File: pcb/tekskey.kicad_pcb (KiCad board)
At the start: 2 copper layers, 123.8 x 128.6 mm, 97 parts, among them SW0 MX_SW_HS, SW1 MX_SW_HS, SW10 MX_SW_HS, SW11 MX_SW_HS, SW12 MX_SW_HS, SW13 MX_SW_HS, SW14 MX_SW_HS, SW15 MX_SW_HS, SW1B1 MX_SW_HS, SW2 MX_SW_HS, SW20 MX_SW_HS, SW21 MX_SW_HS, SW22 MX_SW_HS, SW23 MX_SW_HS, SW24 MX_SW_HS, SW25 MX_SW_HS, SW2B1 MX_SW_HS, SW3 MX_SW_HS, SW30 MX_SW_HS, SW31 MX_SW_HS, SW32 MX_SW_HS, SW33 MX_SW_HS, SW34 MX_SW_HS, SW35 MX_SW_HS, SW3B1 MX_SW_HS, SW4 MX_SW_HS, SW40 MX_SW_HS, SW41 MX_SW_HS, SW42 MX_SW_HS, SW43 MX_SW_HS, SW44 MX_SW_HS, SW45 MX_SW_HS, SW4B1 MX_SW_HS, SW5 MX_SW_HS, SW50 MX_SW_HS, SW51 MX_SW_HS, SW51B1 MX_SW_HS, SW52 MX_SW_HS, SW53 MX_SW_HS, SW54 MX_SW_HS, SW55 MX_SW_HS, SW55B1 MX_SW_HS, SW5B1 MX_SW_HS

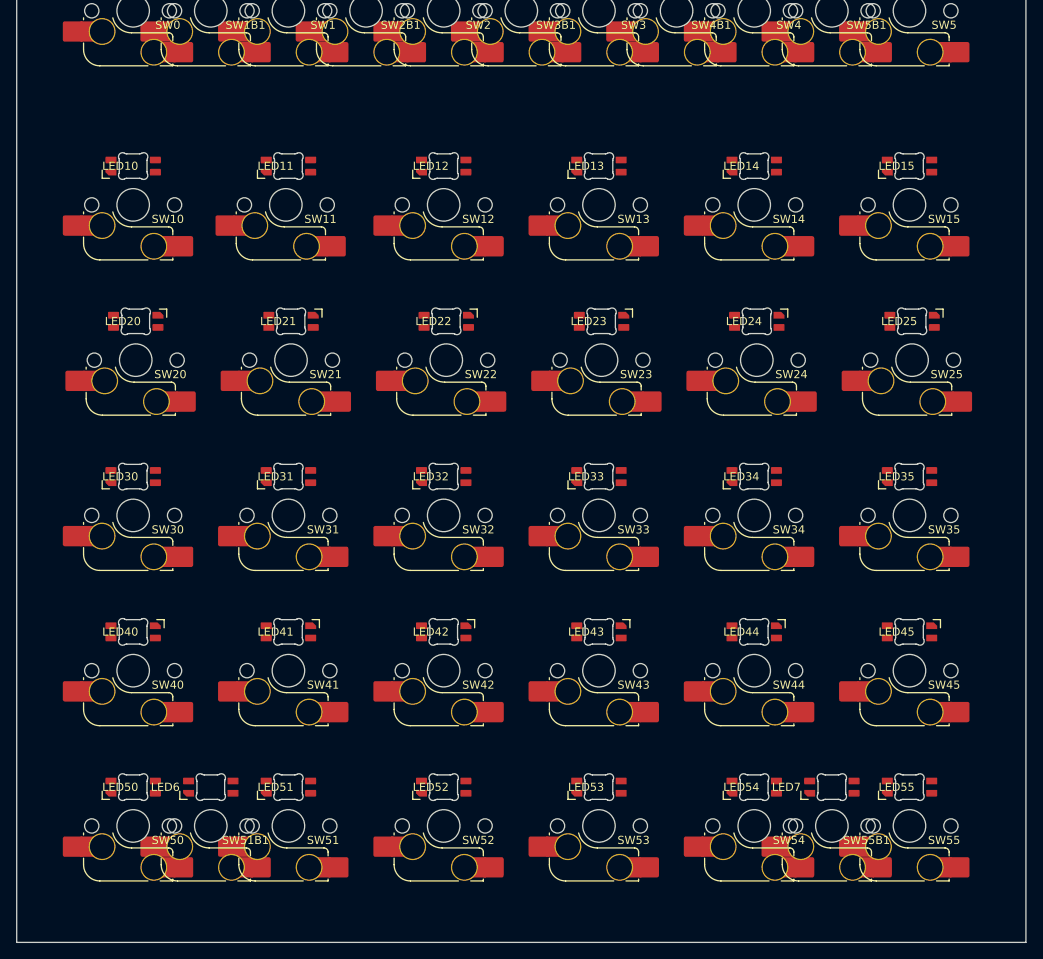
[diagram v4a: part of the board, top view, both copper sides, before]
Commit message: add through hole diodes
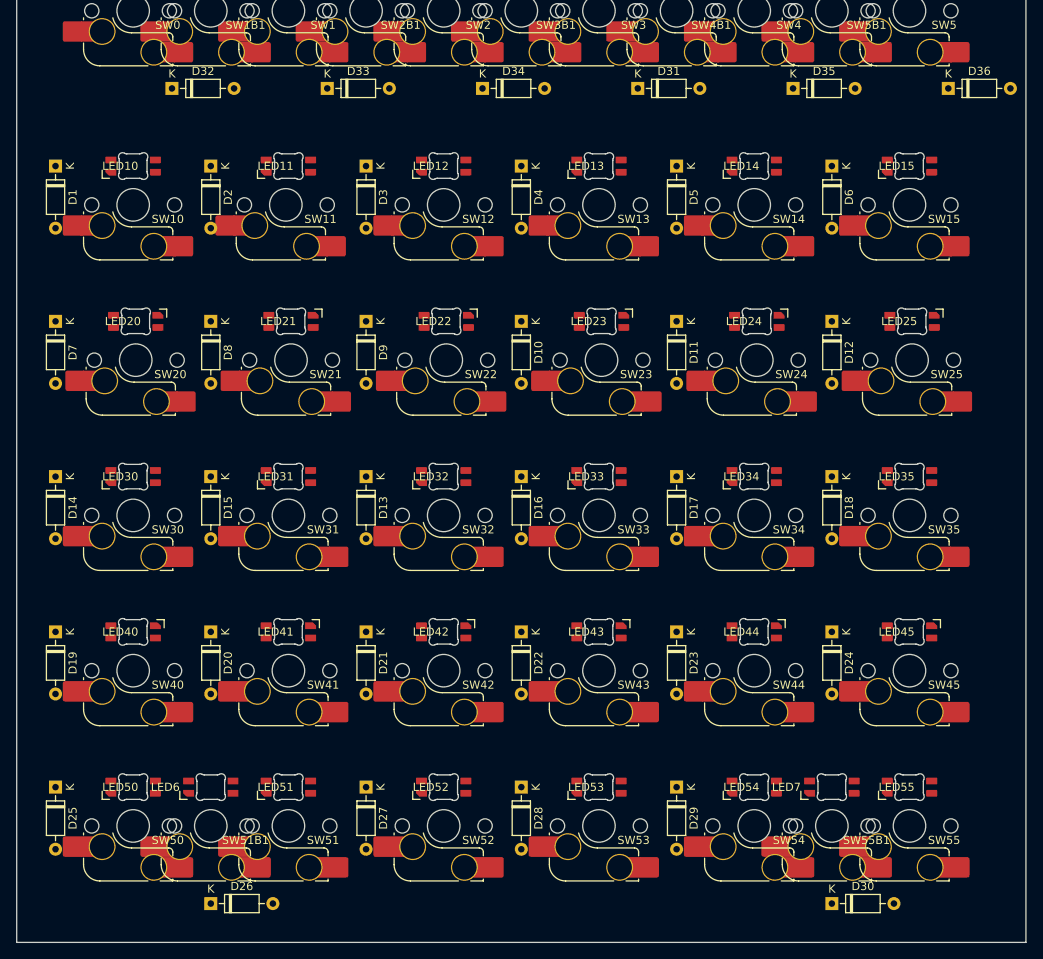
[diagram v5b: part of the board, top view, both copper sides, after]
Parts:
- added D1: 1N4148, Diode_THT:D_DO-35_SOD27_P7.62mm_Horizontal, F.Cu at (38.1, 57.1)
- added D10: 1N4148, Diode_THT:D_DO-35_SOD27_P7.62mm_Horizontal, F.Cu at (95.2, 76.2)
- added D11: 1N4148, Diode_THT:D_DO-35_SOD27_P7.62mm_Horizontal, F.Cu at (114.3, 76.2)
- added D12: 1N4148, Diode_THT:D_DO-35_SOD27_P7.62mm_Horizontal, F.Cu at (133.3, 76.2)
- added D13: 1N4148, Diode_THT:D_DO-35_SOD27_P7.62mm_Horizontal, F.Cu at (76.2, 95.2)
- added D14: 1N4148, Diode_THT:D_DO-35_SOD27_P7.62mm_Horizontal, F.Cu at (38.1, 95.2)
- added D15: 1N4148, Diode_THT:D_DO-35_SOD27_P7.62mm_Horizontal, F.Cu at (57.1, 95.2)
- added D16: 1N4148, Diode_THT:D_DO-35_SOD27_P7.62mm_Horizontal, F.Cu at (95.2, 95.2)
- added D17: 1N4148, Diode_THT:D_DO-35_SOD27_P7.62mm_Horizontal, F.Cu at (114.3, 95.2)
- added D18: 1N4148, Diode_THT:D_DO-35_SOD27_P7.62mm_Horizontal, F.Cu at (133.3, 95.2)
- added D19: 1N4148, Diode_THT:D_DO-35_SOD27_P7.62mm_Horizontal, F.Cu at (38.1, 114.3)
- added D2: 1N4148, Diode_THT:D_DO-35_SOD27_P7.62mm_Horizontal, F.Cu at (57.1, 57.1)
- added D20: 1N4148, Diode_THT:D_DO-35_SOD27_P7.62mm_Horizontal, F.Cu at (57.1, 114.3)
- added D21: 1N4148, Diode_THT:D_DO-35_SOD27_P7.62mm_Horizontal, F.Cu at (76.2, 114.3)
- added D22: 1N4148, Diode_THT:D_DO-35_SOD27_P7.62mm_Horizontal, F.Cu at (95.2, 114.3)
- added D23: 1N4148, Diode_THT:D_DO-35_SOD27_P7.62mm_Horizontal, F.Cu at (114.3, 114.3)
- added D24: 1N4148, Diode_THT:D_DO-35_SOD27_P7.62mm_Horizontal, F.Cu at (133.3, 114.3)
- added D25: 1N4148, Diode_THT:D_DO-35_SOD27_P7.62mm_Horizontal, F.Cu at (38.1, 133.3)
- added D26: 1N4148, Diode_THT:D_DO-35_SOD27_P7.62mm_Horizontal, F.Cu at (57.1, 147.6)
- added D27: 1N4148, Diode_THT:D_DO-35_SOD27_P7.62mm_Horizontal, F.Cu at (76.2, 133.3)
- added D28: 1N4148, Diode_THT:D_DO-35_SOD27_P7.62mm_Horizontal, F.Cu at (95.2, 133.3)
- added D29: 1N4148, Diode_THT:D_DO-35_SOD27_P7.62mm_Horizontal, F.Cu at (114.3, 133.3)
- added D3: 1N4148, Diode_THT:D_DO-35_SOD27_P7.62mm_Horizontal, F.Cu at (76.2, 57.1)
- added D30: 1N4148, Diode_THT:D_DO-35_SOD27_P7.62mm_Horizontal, F.Cu at (133.3, 147.6)
- added D31: 1N4148, Diode_THT:D_DO-35_SOD27_P7.62mm_Horizontal, F.Cu at (109.5, 47.6)
- added D32: 1N4148, Diode_THT:D_DO-35_SOD27_P7.62mm_Horizontal, F.Cu at (52.4, 47.6)
- added D33: 1N4148, Diode_THT:D_DO-35_SOD27_P7.62mm_Horizontal, F.Cu at (71.4, 47.6)
- added D34: 1N4148, Diode_THT:D_DO-35_SOD27_P7.62mm_Horizontal, F.Cu at (90.5, 47.6)
- added D35: 1N4148, Diode_THT:D_DO-35_SOD27_P7.62mm_Horizontal, F.Cu at (128.6, 47.6)
- added D36: 1N4148, Diode_THT:D_DO-35_SOD27_P7.62mm_Horizontal, F.Cu at (147.6, 47.6)
- added D4: 1N4148, Diode_THT:D_DO-35_SOD27_P7.62mm_Horizontal, F.Cu at (95.2, 57.1)
- added D5: 1N4148, Diode_THT:D_DO-35_SOD27_P7.62mm_Horizontal, F.Cu at (114.3, 57.1)
- added D6: 1N4148, Diode_THT:D_DO-35_SOD27_P7.62mm_Horizontal, F.Cu at (133.3, 57.1)
- added D7: 1N4148, Diode_THT:D_DO-35_SOD27_P7.62mm_Horizontal, F.Cu at (38.1, 76.2)
- added D8: 1N4148, Diode_THT:D_DO-35_SOD27_P7.62mm_Horizontal, F.Cu at (57.1, 76.2)
- added D9: 1N4148, Diode_THT:D_DO-35_SOD27_P7.62mm_Horizontal, F.Cu at (76.2, 76.2)
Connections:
- SW0 pad 2: row0 -> Net-(SW0-Pad2)
- SW1 pad 2: row0 -> Net-(SW1-Pad2)
- SW10 pad 1: col0 -> Net-(SW10-Pad1)
- SW11 pad 1: col1 -> Net-(SW11-Pad1)
- SW12 pad 1: col2 -> Net-(SW12-Pad1)
- SW13 pad 1: col3 -> Net-(SW13-Pad1)
- SW14 pad 1: col4 -> Net-(SW14-Pad1)
- SW15 pad 1: col5 -> Net-(SW15-Pad1)
- SW1B1 pad 1: row0 -> Net-(SW1-Pad2)
- SW2 pad 2: row0 -> Net-(SW2-Pad2)
- SW20 pad 1: col0 -> Net-(SW20-Pad1)
- SW21 pad 1: col1 -> Net-(SW21-Pad1)
- SW22 pad 1: col2 -> Net-(SW22-Pad1)
- SW23 pad 1: col3 -> Net-(SW23-Pad1)
- SW24 pad 1: col4 -> Net-(SW24-Pad1)
- SW25 pad 1: col5 -> Net-(SW25-Pad1)
- SW2B1 pad 1: row0 -> Net-(SW2-Pad2)
- SW3 pad 2: row0 -> Net-(SW3-Pad2)
- SW30 pad 1: col0 -> Net-(SW30-Pad1)
- SW31 pad 1: col1 -> Net-(SW31-Pad1)
- SW32 pad 1: col2 -> Net-(SW32-Pad1)
- SW33 pad 1: col3 -> Net-(SW33-Pad1)
- SW34 pad 1: col4 -> Net-(SW34-Pad1)
- SW35 pad 1: col5 -> Net-(SW35-Pad1)
- SW3B1 pad 1: row0 -> Net-(SW3-Pad2)
- SW4 pad 2: row0 -> Net-(SW4-Pad2)
- SW40 pad 1: col0 -> Net-(SW40-Pad1)
- SW41 pad 1: col1 -> Net-(SW41-Pad1)
- SW42 pad 1: col2 -> Net-(SW42-Pad1)
- SW43 pad 1: col3 -> Net-(SW43-Pad1)
- SW44 pad 1: col4 -> Net-(SW44-Pad1)
- SW45 pad 1: col5 -> Net-(SW45-Pad1)
- SW4B1 pad 1: row0 -> Net-(SW4-Pad2)
- SW5 pad 2: row0 -> Net-(SW5-Pad2)
- SW50 pad 1: col0 -> Net-(SW50-Pad1)
- SW51 pad 1: col1 -> Net-(SW51B1-Pad1)
- SW51B1 pad 1: row5 -> Net-(SW51B1-Pad1)
- SW51B1 pad 2: col1 -> row5
- SW52 pad 1: col2 -> Net-(SW52-Pad1)
- SW53 pad 1: col3 -> Net-(SW53-Pad1)
- SW54 pad 1: col4 -> Net-(SW54-Pad1)
- SW55 pad 1: col5 -> Net-(SW55B1-Pad1)
- SW55B1 pad 1: row5 -> Net-(SW55B1-Pad1)
- SW55B1 pad 2: col5 -> row5
- SW5B1 pad 1: row0 -> Net-(SW5-Pad2)

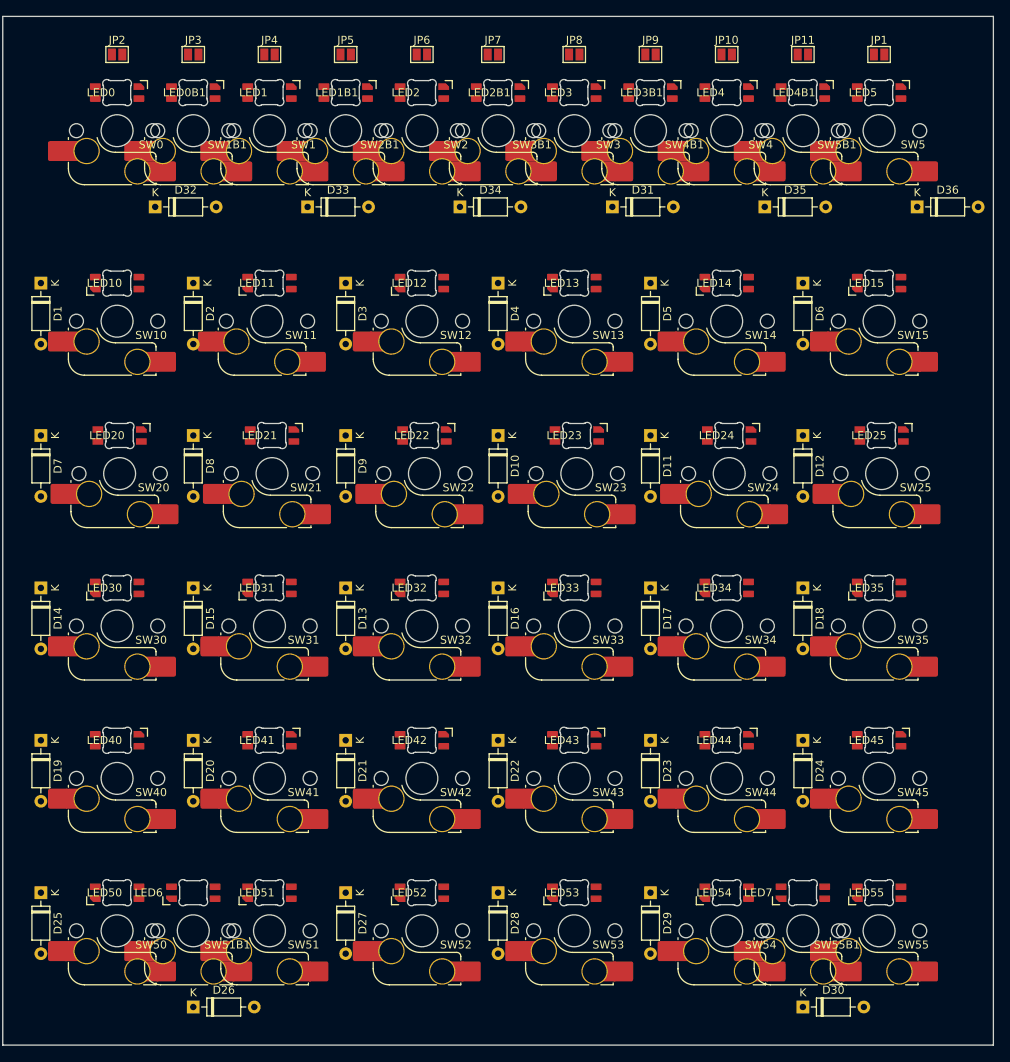
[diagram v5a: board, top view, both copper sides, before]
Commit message: align switches
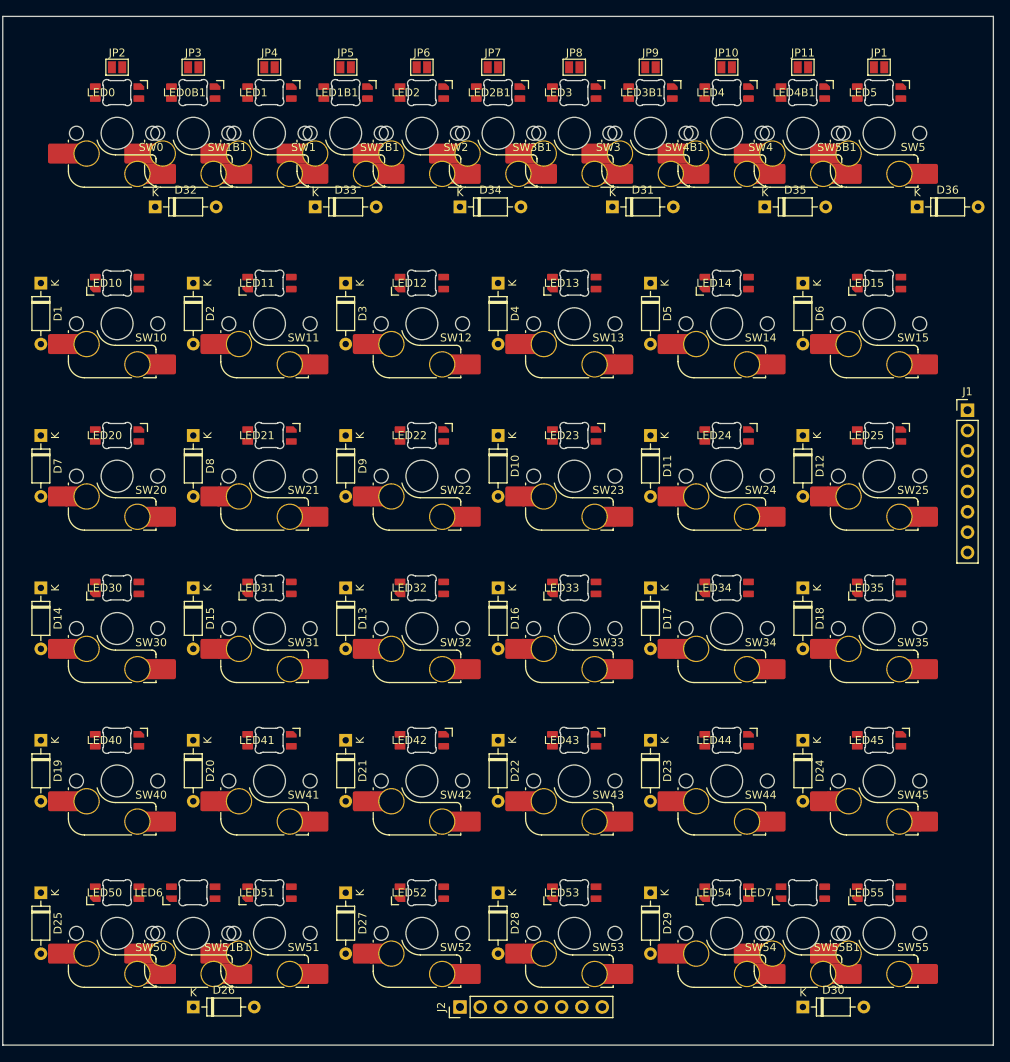
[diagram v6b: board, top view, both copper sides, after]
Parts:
- added J1: Conn_01x08, Connector_PinHeader_2.54mm:PinHeader_1x08_P2.54mm_Vertical, F.Cu at (153.9, 73.0)
- added J2: Conn_01x08, Connector_PinHeader_2.54mm:PinHeader_1x08_P2.54mm_Vertical, F.Cu at (90.5, 147.6)
- moved JP1 1.59 mm to (142.9, 30.2)
- moved JP10 1.59 mm to (123.8, 30.2)
- moved JP11 1.59 mm to (133.3, 30.2)
- moved JP2 1.59 mm to (47.6, 30.2)
- moved JP3 1.59 mm to (57.1, 30.2)
- moved JP4 1.59 mm to (66.7, 30.2)
- moved JP5 1.59 mm to (76.2, 30.2)
- moved JP6 1.59 mm to (85.7, 30.2)
- moved JP7 1.59 mm to (94.6, 30.2)
- moved JP8 1.59 mm to (104.8, 30.2)
- moved JP9 1.59 mm to (114.3, 30.2)
- moved D33 0.95 mm to (72.4, 47.6)
- moved SW21 0.45 mm to (66.7, 81.3)
- moved SW22 0.45 mm to (85.7, 81.3)
- moved SW20 0.45 mm to (47.6, 81.3)
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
